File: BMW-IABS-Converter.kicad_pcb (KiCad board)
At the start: 2 copper layers, 45 parts, among them J1 SWD, J2 HCCPHPE24BKA90F, Q1 IRLML0060TRPbF, Q2 IRLML0060TRPbF, Q4 IRFR9024, Q6 IRFR9024, U1 SN65HVD230, U2 STM32F042F4P6, U3 MC34063AD, U4 LM2904

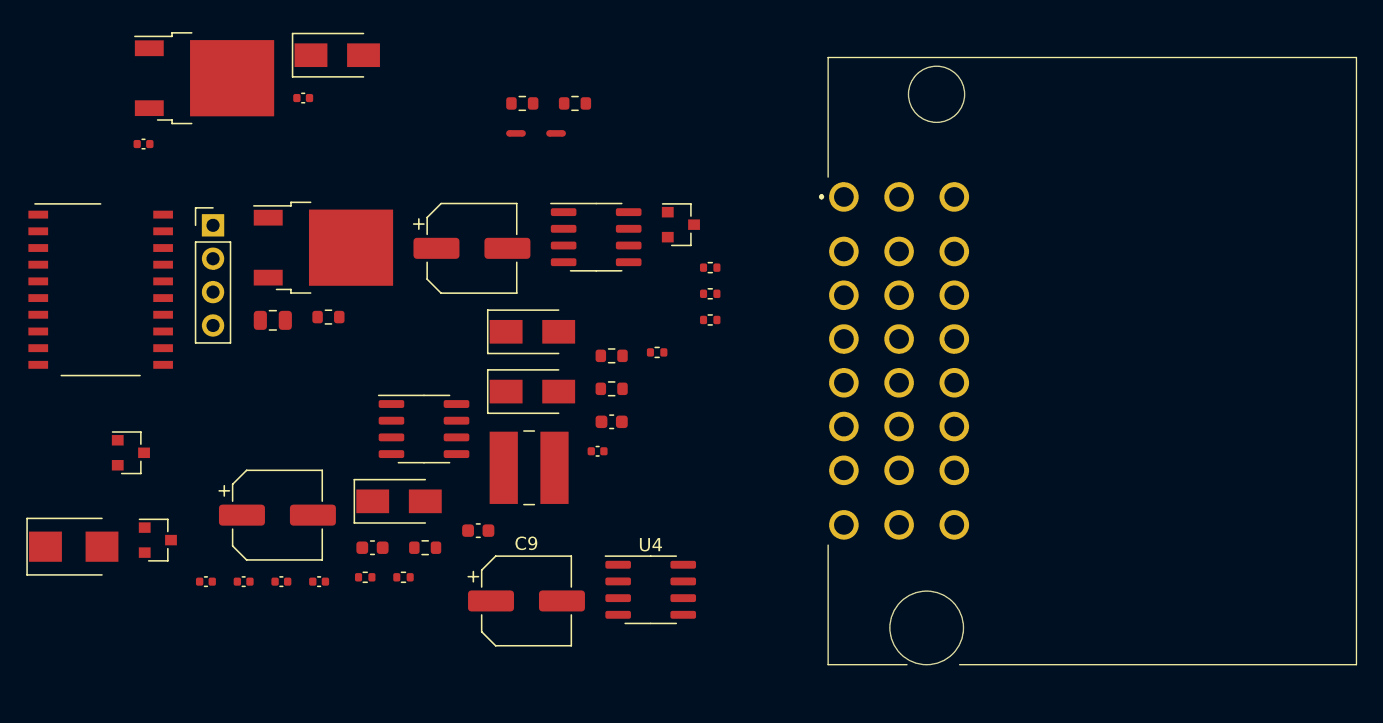
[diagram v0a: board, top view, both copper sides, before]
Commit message: Updated schematic and layout
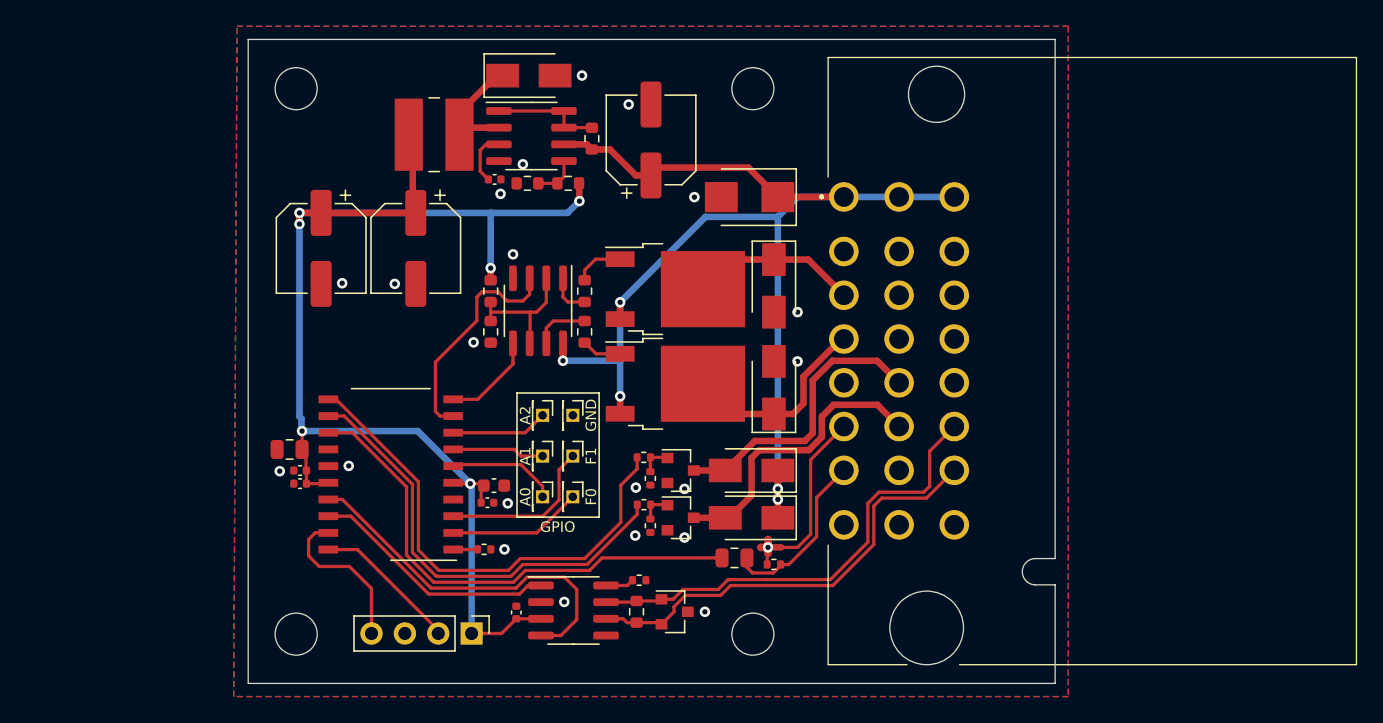
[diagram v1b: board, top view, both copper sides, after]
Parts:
- removed NT1: 15 Tie, NetTie:NetTie-2_SMD_Pad0.5mm
- added D7: US1M, Diode_SMD:D_SMA, F.Cu at (165.4, 109.4)
- added H1: MountingHole, MountingHole:MountingHole_3.2mm_M3, F.Cu at (130.8, 76.8)
- added H2: MountingHole, MountingHole:MountingHole_3.2mm_M3, F.Cu at (130.8, 118.2)
- added H3: MountingHole, MountingHole:MountingHole_3.2mm_M3, F.Cu at (165.5, 76.8)
- added H4: MountingHole, MountingHole:MountingHole_3.2mm_M3, F.Cu at (165.5, 118.2)
- added J3: GPIO_A0, Connector_PinHeader_1.27mm:PinHeader_1x01_P1.27mm_Vertical, F.Cu at (149.5, 107.8)
- added J4: GPIO_A1, Connector_PinHeader_1.27mm:PinHeader_1x01_P1.27mm_Vertical, F.Cu at (149.5, 104.7)
- added J5: GPIO_F0, Connector_PinHeader_1.27mm:PinHeader_1x01_P1.27mm_Vertical, F.Cu at (151.8, 107.8)
- added J6: GPIO_F1, Connector_PinHeader_1.27mm:PinHeader_1x01_P1.27mm_Vertical, F.Cu at (151.8, 104.7)
- added J7: GPIO_A2, Connector_PinHeader_1.27mm:PinHeader_1x01_P1.27mm_Vertical, F.Cu at (149.5, 101.6)
- added J8: GND, Connector_PinHeader_1.27mm:PinHeader_1x01_P1.27mm_Vertical, F.Cu at (151.8, 101.6)
- added LOGO1: Logo_Open_Hardware_Small, Symbol:OSHW-Symbol_6.7x6mm_SilkScreen, B.Cu at (151.3, 97.5)
- added LOGO2: Sine_Logo_S, sine:sine_logo_small, B.Cu at (132.2, 112.2)
- C11: footprint Capacitor_SMD:C_0603_1608Metric -> Capacitor_SMD:C_0805_2012Metric
- C6: footprint Capacitor_SMD:C_0603_1608Metric -> Capacitor_SMD:C_0402_1005Metric
- L1: value 47uH (SND0504-470M) -> 18uH (SND0504-180M)
- Q1, Q2: value IRLML0060TRPbF -> IRLML0030TRPbF
- R13, R14: footprint Capacitor_SMD:C_0402_1005Metric -> Resistor_SMD:R_0603_1608Metric
- R17: footprint Capacitor_SMD:C_0402_1005Metric -> Resistor_SMD:R_0402_1005Metric
- R7, R8: value 10R -> 100R
- moved D5 57.9 mm to (165.2, 85.0), turned to 180 degrees
- moved D1 43.1 mm to (159.6, 116.5)
- moved Q2 39.8 mm to (160.0, 109.4)
- moved Q6 39.3 mm to (159.6, 92.0)
- moved D6 37.6 mm to (167.1, 91.8), turned to 270 degrees
- moved R17 37.5 mm to (167.1, 113.0), turned to 180 degrees
- moved J1 36.8 mm to (144.1, 118.2), turned to 270 degrees
- moved R13 36.5 mm to (152.7, 95.2), turned to 90 degrees
- moved NT2 35.6 mm to (167.2, 111.7), turned to 180 degrees
- moved R3 32.4 mm to (156.7, 116.5), turned to 270 degrees
- moved C9 31.0 mm to (132.7, 88.9), turned to 270 degrees
- moved D4 29.8 mm to (167.1, 99.5), turned to 90 degrees
- moved R5 28.8 mm to (148.3, 84.0)
- moved Q4 28.7 mm to (159.6, 99.2)
- moved R2 27.5 mm to (145.1, 111.8)
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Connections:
- D1 pad 1: /CAN_L -> /CAN_H
- D1 pad 2: /CAN_H -> /CAN_L
- D3 pad 1: /15U -> +12V
- J2 pad A2: /15U -> (no net)
- J2 pad A3: /ABS-WR -> /54
- J2 pad A4: /ABS-W -> /58RL
- J2 pad A6: (no net) -> /TA-
- J2 pad A7: (no net) -> /TAS
- J2 pad B4: /CAN_H -> (no net)
- J2 pad B5: /CAN_L -> /ABS-WR
- J2 pad B6: /TA- -> /ABS-W
- J2 pad B7: /TAS -> (no net)
- J2 pad C2: /54 -> (no net)
- J2 pad C3: /58RL -> (no net)
- J2 pad C6: (no net) -> /CAN_H
- J2 pad C7: (no net) -> /CAN_L
- U2 pad 11: /GEN_WARN -> /ABS_WARN_RLY
- U2 pad 12: /ABS_WARN_RLY -> /GEN_WARN
- U2 pad 2: (no net) -> /GPIO_F0
- U2 pad 3: (no net) -> /GPIO_F1
- U2 pad 6: (no net) -> /GPIO_A0
- U2 pad 7: (no net) -> /GPIO_A1
- U2 pad 8: /SPEED_PWM -> /GPIO_A2
- U4 pad 1: Net-(R13-Pad2) -> Net-(R14-Pad2)
- U4 pad 3: /TAIL_LIGHT -> /BRAKE_LIGHT
- U4 pad 5: /BRAKE_LIGHT -> /TAIL_LIGHT
- U4 pad 7: Net-(R14-Pad2) -> Net-(R13-Pad2)
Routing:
- net +3V3: track 0.00 -> 101.9 mm, vias 0 -> 6
- net +12V: track 0.00 -> 93.1 mm, vias 0 -> 5
- net /SPEED_PWM: track 0.00 -> 38.5 mm
- net /ABS_WARN_RLY: track 0.00 -> 37.7 mm
- net /CAN_H: track 0.00 -> 35.3 mm
- net /GEN_WARN: track 0.00 -> 34.3 mm
- net /CAN_L: track 0.00 -> 33.5 mm
- net /CAN_RX: track 0.00 -> 27.9 mm
- net /ABS-W: track 0.00 -> 22.5 mm
- net /ABS-WR: track 0.00 -> 22.2 mm
- net /CAN_TX: track 0.00 -> 18.9 mm
- net /BRAKE_LIGHT: track 0.00 -> 17.4 mm
- net /58RL: track 0.00 -> 15.2 mm
- net /TAS: track 0.00 -> 13.3 mm
- net /54: track 0.00 -> 12.8 mm
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- added copper zone on B.Cu, net GND
- added copper zone on F.Cu, net GND
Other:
- board outline added: 61.4 x 49 mm
- net class Power added: clearance 0.2, trace_width 0.5, via_dia 0.8, via_drill 0.4
- board text added: "BMW iABS-II CAN Interface Rev. A"
- board text added: "GPIO"
- board text added: "sinebureau.com 2021"
